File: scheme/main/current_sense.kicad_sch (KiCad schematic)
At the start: 3 parts, among them U2 ACS712xLCTR-05B

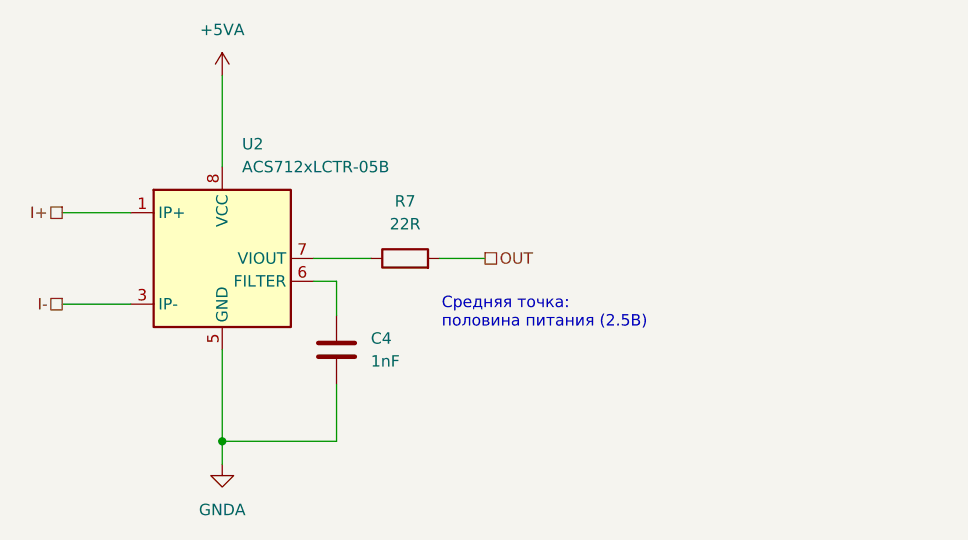
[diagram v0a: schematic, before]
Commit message: added decoupling capacitors
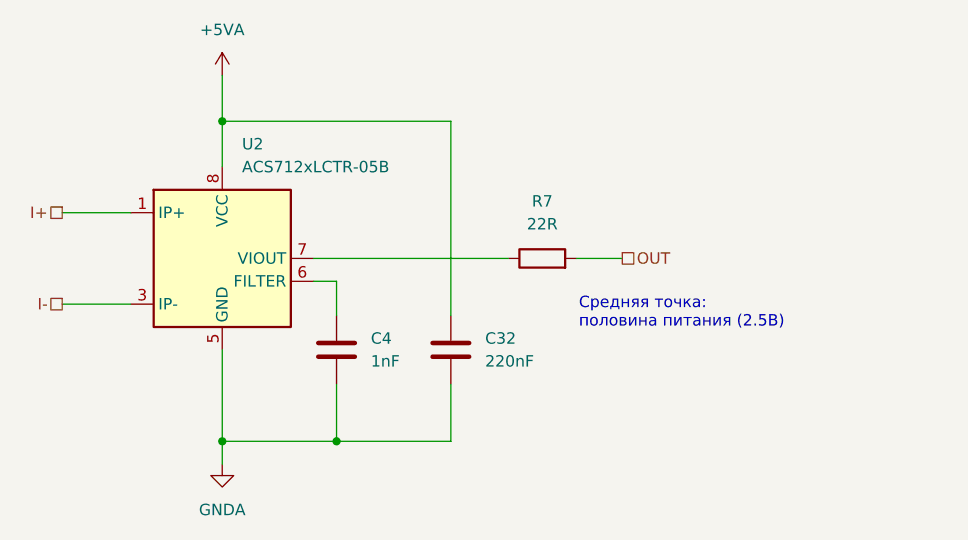
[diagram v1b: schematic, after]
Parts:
- added C32: 220nF, Capacitor_SMD:C_0805_2012Metric, symbol Device:C
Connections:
- net +5VA: now also C32.1
- net GNDA: now also C32.2
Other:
- moved on the sheet: R7
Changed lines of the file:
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@@
 	(paper "A4")
+	(junction
+		(at 119.38 111.76)
+		(diameter 0)
+		(color 0 0 0 0)
+	)
 	(junction
 		(at 106.68 111.76)
@@
 		(color 0 0 0 0)
 	)
+	(junction
+		(at 106.68 76.2)
+		(diameter 0)
+		(color 0 0 0 0)
+	)
+	(wire
+		(pts
+			(xy 106.68 76.2) (xy 106.68 81.28)
+		)
+		(stroke
+			(width 0)
+			(type default)
+		)
+	)
 	(wire
 		(pts
@@
 	(wire
 		(pts
+			(xy 132.08 105.41) (xy 132.08 111.76)
+		)
+		(stroke
+			(width 0)
+			(type default)
+		)
+	)
+	(wire
+		(pts
+			(xy 132.08 97.79) (xy 132.08 76.2)
+		)
+		(stroke
+			(width 0)
+			(type default)
+		)
+	)
+	(wire
+		(pts
 			(xy 106.68 111.76) (xy 106.68 114.3)
 		)
@@
 	(wire
 		(pts
-			(xy 106.68 71.12) (xy 106.68 81.28)
+			(xy 106.68 71.12) (xy 106.68 76.2)
+		)
+		(stroke
+			(width 0)
+			(type default)
+		)
+	)
+	(wire
+		(pts
+			(xy 132.08 111.76) (xy 119.38 111.76)
 		)
 		(stroke
@@
 	(wire
 		(pts
-			(xy 116.84 91.44) (xy 123.19 91.44)
-		)
-		(stroke
-			(width 0)
-			(type default)
-		)
-	)
-	(wire
-		(pts
-			(xy 130.81 91.44) (xy 135.89 91.44)
+			(xy 116.84 91.44) (xy 138.43 91.44)
+		)
+		(stroke
+			(width 0)
+			(type default)
+		)
+	)
+	(wire
+		(pts
+			(xy 146.05 91.44) (xy 151.13 91.44)
+		)
+		(stroke
+			(width 0)
+			(type default)
+		)
+	)
+	(wire
+		(pts
+			(xy 132.08 76.2) (xy 106.68 76.2)
 		)
 		(stroke
@@
 	(text "Средняя точка:\nполовина питания (2.5В)"
 		(exclude_from_sim no)
-		(at 131.064 97.536 0)
+		(at 146.304 97.536 0)
 		(effects
 			(font
@@
 	(hierarchical_label "OUT"
 		(shape passive)
-		(at 135.89 91.44 0)
+		(at 151.13 91.44 0)
 		(effects
 			(font
@@
 	(symbol
 		(lib_id "Device:R")
-		(at 127 91.44 90)
+		(at 142.24 91.44 90)
 		(unit 1)
 		(exclude_from_sim no)
@@
 		(fields_autoplaced yes)
 		(property "Reference" "R7"
-			(at 127 85.09 90)
+			(at 142.24 85.09 90)
 			(effects
 				(font
@@
 		)
 		(property "Value" "22R"
-			(at 127 87.63 90)
+			(at 142.24 87.63 90)
 			(effects
 				(font
@@
 		)
 		(property "Footprint" ""
-			(at 127 93.218 90)
+			(at 142.24 93.218 90)
 			(effects
 				(font
@@
 		)
 		(property "Datasheet" "~"
-			(at 127 91.44 0)
+			(at 142.24 91.44 0)
 			(effects
 				(font
@@
 		)
 		(property "Description" "Resistor"
-			(at 127 91.44 0)
+			(at 142.24 91.44 0)
 			(effects
 				(font
@@
 					(unit 1)
 				)
+			)
+		)
+	)
+	(symbol
+		(lib_id "Device:C")
+		(at 132.08 101.6 0)
+		(unit 1)
+		(exclude_from_sim no)
+		(in_bom yes)
+		(on_board yes)
+		(dnp no)
+		(fields_autoplaced yes)
+		(property "Reference" "C32"
+			(at 135.89 100.3299 0)
+			(effects
+				(font
+					(size 1.27 1.27)
+				)
+				(justify left)
+			)
+		)
+		(property "Value" "220nF"
+			(at 135.89 102.8699 0)
+			(effects
+				(font
+					(size 1.27 1.27)
+				)
+				(justify left)
+			)
+		)
+		(property "Footprint" "Capacitor_SMD:C_0805_2012Metric"
+			(at 133.0452 105.41 0)
+			(effects
+				(font
+					(size 1.27 1.27)
+				)
+				(hide yes)
+			)
+		)
+		(property "Datasheet" "~"
+			(at 132.08 101.6 0)
+			(effects
+				(font
+					(size 1.27 1.27)
+				)
+				(hide yes)
+			)
+		)
+		(property "Description" "Unpolarized capacitor"
+			(at 132.08 101.6 0)
+			(effects
+				(font
+					(size 1.27 1.27)
+				)
+				(hide yes)
+			)
+		)
+		(pin "2"
+		)
+		(pin "1"
+		)
+		(instances
+			(project "main"
+				(path "/c11d1dbc-4db9-4712-8d1d-5f6f7086cded/1bd0e084-5602-43f5-a9de-9167dc3ddabf"
+					(reference "C33")
+					(unit 1)
+				)
+				(path "/c11d1dbc-4db9-4712-8d1d-5f6f7086cded/236c27c1-9285-48af-b94c-0a581f89ad4f"
+					(reference "C32")
+					(unit 1)
+				)
+				(path "/c11d1dbc-4db9-4712-8d1d-5f6f7086cded/eb061644-a076-485c-afde-65b59d5b34e4"
+					(reference "C34")
+					(unit 1)
+				)
